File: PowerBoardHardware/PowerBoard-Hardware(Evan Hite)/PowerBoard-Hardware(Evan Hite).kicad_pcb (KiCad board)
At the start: 2 copper layers, 126 parts, among them Q1 IPT020N10N3, Q10 Q_NMOS_DGS, Q11 Q_NMOS_DGS, Q12 Q_NMOS_DGS, Q13 Q_NMOS_DGS, Q2 IPT020N10N3, Q3 IPT020N10N3, Q4 IPT020N10N3, Q5 IPT020N10N3, Q6 Q_NMOS_DGS, Q7 Q_NMOS_DGS, Q8 Q_NMOS_DGS, Q9 Q_NMOS_DGS, U1 TM4C129E_Launchpad, U10 OKI, U11 LT1910, U12 LT1910, U13 LT1910, U14 LT1910, U15 ATC_FUSE_BLOCK, U16 ATC_FUSE_BLOCK, U17 ATC_FUSE_BLOCK, U18 ATC_FUSE_BLOCK, U2 ATC_FUSE_BLOCK, U23 LT1910, U24 LT1910, U25 LT1910, U26 LT1910, U27 ATC_FUSE_BLOCK, U28 ATC_FUSE_BLOCK, U29 ATC_FUSE_BLOCK, U3 ATC_FUSE_BLOCK, U30 ATC_FUSE_BLOCK, U4 ATC_FUSE_BLOCK, U5 LT1910, U6 LT1910

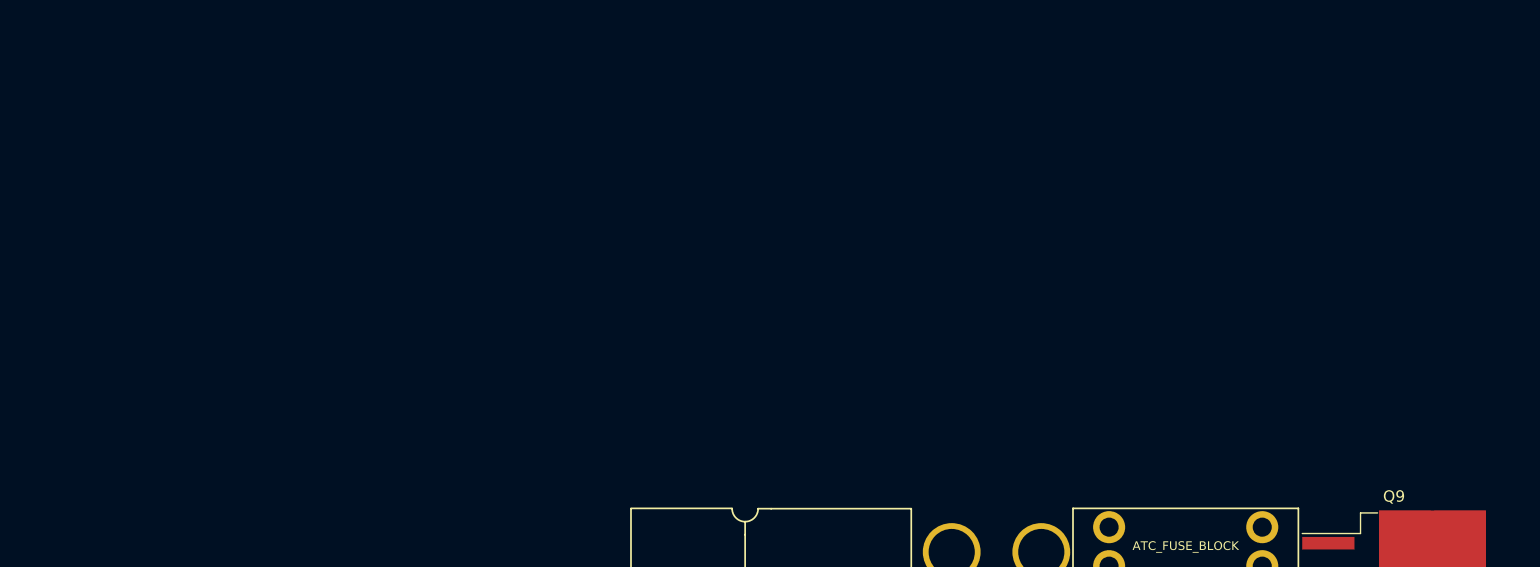
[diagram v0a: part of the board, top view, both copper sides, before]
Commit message: Reassigned Libraries
Reassigned Libraries to make sure everything works after file organization.
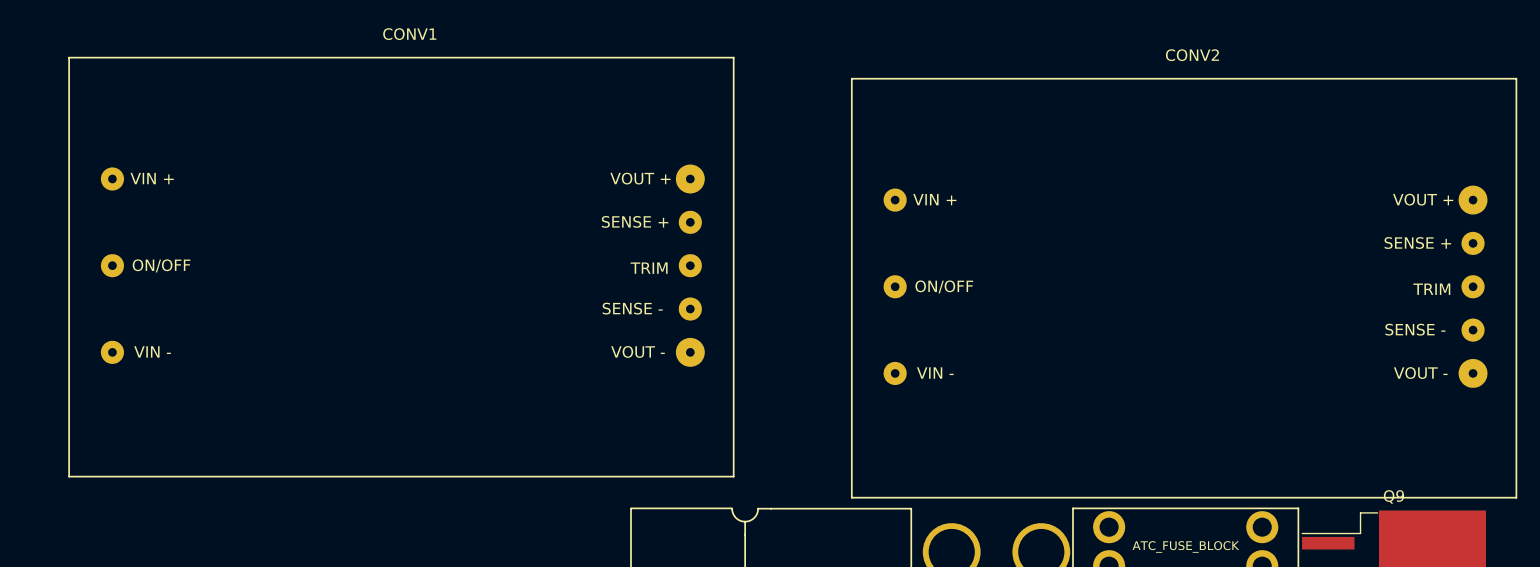
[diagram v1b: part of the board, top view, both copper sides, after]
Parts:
- added CONV1: DC-DC_Converter, DC-DC_Converter_Quarter_Brick:DC-DC_Converter_Quarter_Brick, F.Cu at (177.8, 29.2)
- added CONV2: DC-DC_Converter, DC-DC_Converter_Quarter_Brick:DC-DC_Converter_Quarter_Brick, F.Cu at (246.6, 31.1)
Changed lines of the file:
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@@
     (tracks 0)
     (zones 0)
-    (modules 126)
-    (nets 160)
+    (modules 128)
+    (nets 164)
   )
   (page A4)
@@
     (pad_to_mask_clearance 0.2)
     (aux_axis_origin 0 0)
-    (visible_elements FFFFFF7F)
+    (visible_elements 7FFFFFFF)
     (pcbplotparams
       (layerselection 0x010fc_ffffffff)
@@
   (net 158 "Net-(U26-Pad3)")
   (net 159 "Net-(U26-Pad2)")
+  (net 160 "Net-(CONV1-Pad4)")
+  (net 161 "Net-(CONV1-Pad6)")
+  (net 162 "Net-(CONV2-Pad6)")
+  (net 163 "Net-(CONV2-Pad4)")
   (net_class Default "This is the default net class."
     (clearance 0.2)
@@
     (add_net "Net-(5k8-Pad2)")
     (add_net "Net-(CONV1-Pad2)")
+    (add_net "Net-(CONV1-Pad4)")
+    (add_net "Net-(CONV1-Pad6)")
     (add_net "Net-(CONV2-Pad2)")
+    (add_net "Net-(CONV2-Pad4)")
+    (add_net "Net-(CONV2-Pad6)")
     (add_net "Net-(Q10-Pad2)")
     (add_net "Net-(Q11-Pad2)")
@@
       (net 3 V_BATT))
   )
+  (module DC-DC_Converter_Quarter_Brick:DC-DC_Converter_Quarter_Brick (layer F.Cu)
+    (at 177.8 29.21)
+    (fp_text reference CONV1 (at -24.638 -12.7) (layer F.SilkS)
+      (effects (font (size 1 1) (thickness 0.15)))
+    )
+    (fp_text value DC-DC_Converter (at -24.892 -11.43 180) (layer F.Fab)
+      (effects (font (size 1 1) (thickness 0.15)))
+    )
+    (fp_line (start -54.61 26.162) (end 3.81 26.162) (layer F.SilkS) (width 0.15))
+    (fp_line (start 3.81 -10.668) (end 3.81 26.162) (layer F.SilkS) (width 0.15))
+    (fp_line (start -54.61 -10.668) (end -54.61 26.162) (layer F.SilkS) (width 0.15))
+    (fp_line (start -54.61 -10.668) (end 3.81 -10.668) (layer F.SilkS) (width 0.15))
+    (fp_text user "VIN -" (at -47.244 15.24) (layer F.SilkS)
+      (effects (font (size 1 1) (thickness 0.15)))
+    )
+    (fp_text user ON/OFF (at -46.482 7.62) (layer F.SilkS)
+      (effects (font (size 1 1) (thickness 0.15)))
+    )
+    (fp_text user "VIN +" (at -47.244 0) (layer F.SilkS)
+      (effects (font (size 1 1) (thickness 0.15)))
+    )
+    (fp_text user "VOUT -" (at -4.572 15.24) (layer F.SilkS)
+      (effects (font (size 1 1) (thickness 0.15)))
+    )
+    (fp_text user "VOUT +" (at -4.318 0) (layer F.SilkS)
+      (effects (font (size 1 1) (thickness 0.15)))
+    )
+    (fp_text user "SENSE +" (at -4.826 3.81) (layer F.SilkS)
+      (effects (font (size 1 1) (thickness 0.15)))
+    )
+    (fp_text user TRIM (at -3.556 7.874) (layer F.SilkS)
+      (effects (font (size 1 1) (thickness 0.15)))
+    )
+    (fp_text user "SENSE -" (at -5.08 11.43) (layer F.SilkS)
+      (effects (font (size 1 1) (thickness 0.15)))
+    )
+    (pad 3 thru_hole circle (at -50.8 15.24) (size 2.032 2.032) (drill 0.762) (layers *.Cu *.Mask)
+      (net 1 -BATT))
+    (pad 2 thru_hole circle (at -50.8 7.62) (size 2.032 2.032) (drill 0.762) (layers *.Cu *.Mask)
+      (net 54 "Net-(CONV1-Pad2)"))
+    (pad 1 thru_hole circle (at -50.8 0) (size 2.032 2.032) (drill 0.762) (layers *.Cu *.Mask)
+      (net 3 V_BATT))
+    (pad 4 thru_hole circle (at 0 15.24) (size 2.54 2.54) (drill 0.762) (layers *.Cu *.Mask)
+      (net 160 "Net-(CONV1-Pad4)"))
+    (pad 8 thru_hole circle (at 0 0) (size 2.54 2.54) (drill 0.762) (layers *.Cu *.Mask)
+      (net 34 "Net-(2.2uF1-Pad1)"))
+    (pad 7 thru_hole circle (at 0 3.81) (size 2.032 2.032) (drill 0.762) (layers *.Cu *.Mask)
+      (net 34 "Net-(2.2uF1-Pad1)"))
+    (pad 6 thru_hole circle (at 0 7.62) (size 2.032 2.032) (drill 0.762) (layers *.Cu *.Mask)
+      (net 161 "Net-(CONV1-Pad6)"))
+    (pad 5 thru_hole circle (at 0 11.43) (size 2.032 2.032) (drill 0.762) (layers *.Cu *.Mask)
+      (net 1 -BATT))
+  )
+  (module DC-DC_Converter_Quarter_Brick:DC-DC_Converter_Quarter_Brick (layer F.Cu)
+    (at 246.605001 31.063001)
+    (fp_text reference CONV2 (at -24.638 -12.7) (layer F.SilkS)
+      (effects (font (size 1 1) (thickness 0.15)))
+    )
+    (fp_text value DC-DC_Converter (at -24.892 -11.43 180) (layer F.Fab)
+      (effects (font (size 1 1) (thickness 0.15)))
+    )
+    (fp_text user "SENSE -" (at -5.08 11.43) (layer F.SilkS)
+      (effects (font (size 1 1) (thickness 0.15)))
+    )
+    (fp_text user TRIM (at -3.556 7.874) (layer F.SilkS)
+      (effects (font (size 1 1) (thickness 0.15)))
+    )
+    (fp_text user "SENSE +" (at -4.826 3.81) (layer F.SilkS)
+      (effects (font (size 1 1) (thickness 0.15)))
+    )
+    (fp_text user "VOUT +" (at -4.318 0) (layer F.SilkS)
+      (effects (font (size 1 1) (thickness 0.15)))
+    )
+    (fp_text user "VOUT -" (at -4.572 15.24) (layer F.SilkS)
+      (effects (font (size 1 1) (thickness 0.15)))
+    )
+    (fp_text user "VIN +" (at -47.244 0) (layer F.SilkS)
+      (effects (font (size 1 1) (thickness 0.15)))
+    )
+    (fp_text user ON/OFF (at -46.482 7.62) (layer F.SilkS)
+      (effects (font (size 1 1) (thickness 0.15)))
+    )
+    (fp_text user "VIN -" (at -47.244 15.24) (layer F.SilkS)
+      (effects (font (size 1 1) (thickness 0.15)))
+    )
+    (fp_line (start -54.61 -10.668) (end 3.81 -10.668) (layer F.SilkS) (width 0.15))
+    (fp_line (start -54.61 -10.668) (end -54.61 26.162) (layer F.SilkS) (width 0.15))
+    (fp_line (start 3.81 -10.668) (end 3.81 26.162) (layer F.SilkS) (width 0.15))
+    (fp_line (start -54.61 26.162) (end 3.81 26.162) (layer F.SilkS) (width 0.15))
+    (pad 5 thru_hole circle (at 0 11.43) (size 2.032 2.032) (drill 0.762) (layers *.Cu *.Mask)
+      (net 1 -BATT))
+    (pad 6 thru_hole circle (at 0 7.62) (size 2.032 2.032) (drill 0.762) (layers *.Cu *.Mask)
+      (net 162 "Net-(CONV2-Pad6)"))
+    (pad 7 thru_hole circle (at 0 3.81) (size 2.032 2.032) (drill 0.762) (layers *.Cu *.Mask)
+      (net 36 "Net-(330uF5-Pad1)"))
+    (pad 8 thru_hole circle (at 0 0) (size 2.54 2.54) (drill 0.762) (layers *.Cu *.Mask)
+      (net 36 "Net-(330uF5-Pad1)"))
+    (pad 4 thru_hole circle (at 0 15.24) (size 2.54 2.54) (drill 0.762) (layers *.Cu *.Mask)
+      (net 163 "Net-(CONV2-Pad4)"))
+    (pad 1 thru_hole circle (at -50.8 0) (size 2.032 2.032) (drill 0.762) (layers *.Cu *.Mask)
+      (net 3 V_BATT))
+    (pad 2 thru_hole circle (at -50.8 7.62) (size 2.032 2.032) (drill 0.762) (layers *.Cu *.Mask)
+      (net 55 "Net-(CONV2-Pad2)"))
+    (pad 3 thru_hole circle (at -50.8 15.24) (size 2.032 2.032) (drill 0.762) (layers *.Cu *.Mask)
+      (net 1 -BATT))
+  )
 )

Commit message: Updated Layout
Basic Layout Positioning has begun. DC-DC converters placed. Logic, Actuation, and Communication are placed. One motor has been placed. The rest will be placed at a later time.
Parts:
- added REF**: BATT_PWR_VIA, MRDT-Drill_Holes:BATT_PWR_VIA, F.Cu at (152.9, 128.3)
- added REF**: BATT_PWR_VIA, MRDT-Drill_Holes:BATT_PWR_VIA, F.Cu at (198.6, 128.3)
- added U19: ACS714xLCTR-05B, Housings_SOIC:SOIC-8_3.9x4.9mm_Pitch1.27mm, F.Cu at (255.3, 109.2)
- added U20: ACS714xLCTR-05B, Housings_SOIC:SOIC-8_3.9x4.9mm_Pitch1.27mm, F.Cu at (232.2, 85.2)
- added U21: ACS714xLCTR-05B, Housings_SOIC:SOIC-8_3.9x4.9mm_Pitch1.27mm, F.Cu at (229.9, 194.3)
- added U22: ACS714xLCTR-05B, Housings_SOIC:SOIC-8_3.9x4.9mm_Pitch1.27mm, F.Cu at (229.9, 189.2)
- added U31: ACS714xLCTR-05B, Housings_SOIC:SOIC-8_3.9x4.9mm_Pitch1.27mm, F.Cu at (229.9, 226.1)
- added U32: ACS714xLCTR-05B, Housings_SOIC:SOIC-8_3.9x4.9mm_Pitch1.27mm, F.Cu at (229.9, 221.0)
- added U33: ACS714xLCTR-05B, Housings_SOIC:SOIC-8_3.9x4.9mm_Pitch1.27mm, F.Cu at (229.9, 215.9)
- added U34: ACS714xLCTR-05B, Housings_SOIC:SOIC-8_3.9x4.9mm_Pitch1.27mm, F.Cu at (229.7, 211.2)
- added U7: ACS714xLCTR-05B, Housings_SOIC:SOIC-8_3.9x4.9mm_Pitch1.27mm, F.Cu at (158.8, 20.3)
- added U8: ACS714xLCTR-05B, Housings_SOIC:SOIC-8_3.9x4.9mm_Pitch1.27mm, F.Cu at (224.8, 26.7)
- added U9: ACS714xLCTR-05B, Housings_SOIC:SOIC-8_3.9x4.9mm_Pitch1.27mm, F.Cu at (179.1, 19.1)
- added VCC1: AndersonPP, MRDT-Connectors:Anderson_2_Vertical, F.Cu at (141.7, 24.9)
- added VCC10: AndersonPP, MRDT-Connectors:Anderson_2_Vertical, F.Cu at (27.9, 114.3)
- added VCC11: AndersonPP, MRDT-Connectors:Anderson_2_Vertical, F.Cu at (27.9, 129.5)
- added VCC2: AndersonPP, MRDT-Connectors:Anderson_2_Vertical, F.Cu at (188.2, 24.9)
- added VCC3: AndersonPP, MRDT-Connectors:Anderson_2_Vertical, F.Cu at (236.0, 24.9)
- added VCC4: AndersonPP, MRDT-Connectors:Anderson_2_Vertical, F.Cu at (274.3, 83.8)
- added VCC5: AndersonPP, MRDT-Connectors:Anderson_2_Vertical, F.Cu at (274.3, 102.9)
- added VCC6: AndersonPP, MRDT-Connectors:Anderson_2_Vertical, F.Cu at (274.3, 114.3)
- added VCC7: AndersonPP, MRDT-Connectors:Anderson_2_Vertical, F.Cu at (274.3, 129.5)
- added VCC8: AndersonPP, MRDT-Connectors:Anderson_2_Vertical, F.Cu at (27.9, 83.8)
- added VCC9: AndersonPP, MRDT-Connectors:Anderson_2_Vertical, F.Cu at (27.9, 99.1)
- moved U30 325.1 mm to (372.1, 148.6)
- moved U28 265.4 mm to (351.8, 141.0)
- moved 1.5KE36A2 260.7 mm to (387.4, 121.9)
- moved 1.5KE36A1 239.9 mm to (375.9, 121.9)
- moved U17 206.7 mm to (331.5, 141.0)
- moved Conn5 206.5 mm to (274.3, 102.9), turned to 180 degrees
- moved U27 206.4 mm to (331.5, 148.6)
- moved Conn6 200.7 mm to (274.3, 114.3), turned to 180 degrees
- moved Q12 190.6 mm to (341.9, 184.4)
- moved Conn10 178.4 mm to (27.9, 114.3)
- moved Conn4 177.0 mm to (274.3, 83.8), turned to 180 degrees
- moved 3V3FAN1 165.5 mm to (24.1, 73.7), turned to 90 degrees
- moved 5k1 164.4 mm to (270.5, 73.7)
- moved U2 163.6 mm to (177.8, 49.5), turned to 90 degrees
- moved 1k3 162.2 mm to (227.3, 20.3), turned to 90 degrees
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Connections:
- net -BATT renamed GND
- 0.1uF2 pad 1: V_BATT -> PVDD
- 1.5KE36A1 pad 1: V_BATT -> PVDD
- 1.5KE36A2 pad 1: V_BATT -> PVDD
- 100k3 pad 1: V_BATT -> PVDD
- 10uF2 pad 1: V_BATT -> PVDD
- 1mF1 pad 1: V_BATT -> PVDD
- 1mF2 pad 1: V_BATT -> PVDD
- 1mF3 pad 1: V_BATT -> PVDD
- 1mF4 pad 1: V_BATT -> PVDD
- 1nF2 pad 1: V_BATT -> PVDD
- CONV1 pad 1: V_BATT -> PVDD
- CONV2 pad 1: V_BATT -> PVDD
- U10 pad 1: V_BATT -> PVDD
- U15 pad 1: V_BATT -> PVDD
- U15 pad 2: V_BATT -> Net-(U15-Pad2)
- U16 pad 1: V_BATT -> PVDD
- U16 pad 2: V_BATT -> Net-(U16-Pad2)
- U17 pad 1: V_BATT -> PVDD
- U17 pad 2: V_BATT -> Net-(U17-Pad2)
- U18 pad 1: V_BATT -> PVDD
- U18 pad 2: V_BATT -> Net-(U18-Pad2)
- U2 pad 2: Net-(2.2uF1-Pad1) -> Net-(Q5-Pad3)
- U27 pad 1: V_BATT -> PVDD
- U27 pad 2: V_BATT -> Net-(U27-Pad2)
- U28 pad 1: V_BATT -> PVDD
- U28 pad 2: V_BATT -> Net-(U28-Pad2)
- U29 pad 1: V_BATT -> PVDD
- U29 pad 2: V_BATT -> Net-(U29-Pad2)
- U3 pad 2: Net-(330uF5-Pad1) -> Net-(2.2uF3-Pad1)
- U30 pad 1: V_BATT -> PVDD
- U30 pad 2: V_BATT -> Net-(U30-Pad2)
- U4 pad 2: Net-(2.2uF1-Pad1) -> Net-(Q4-Pad3)
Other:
- copper layers 2 -> 4
- board text added: "<------ Tiva Line Up"

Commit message: 1st Placement is complete
The first placement is now complete, traces still need to be added. The schematic was updated with the placement of Andersons. Certain andersons were in the wrong areas on the schematic. Silkscreen of each motor needs to be added. Outline of board is now in edge cuts.
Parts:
- moved Q12 306.1 mm to (53.7, 81.5)
- moved Q13 297.6 mm to (53.3, 96.5)
- moved Q11 275.5 mm to (53.3, 111.8)
- moved Q10 274.9 mm to (53.7, 127.2)
- moved U30 268.5 mm to (108.0, 100.3), turned to 90 degrees
- moved 1.5KE36A1 259.1 mm to (116.8, 123.2), turned to 270 degrees
- moved 1.5KE36A2 259.1 mm to (128.3, 123.2), turned to 270 degrees
- moved U28 255.4 mm to (99.1, 104.1), turned to 90 degrees
- moved U27 236.6 mm to (99.1, 104.1), turned to 270 degrees
- moved U29 235.0 mm to (82.5, 94.0), turned to 270 degrees
- moved D11 222.4 mm to (15.1, 76.2)
- moved D10 213.3 mm to (15.2, 92.7)
- moved 1mF1 211.0 mm to (119.4, 96.5), turned to 180 degrees
- moved D9 207.9 mm to (15.2, 108.0)
- moved 1mF4 203.4 mm to (128.3, 96.5)
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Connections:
- VCC10 pad 2: Net-(5k8-Pad2) -> Net-(5k6-Pad2)
- VCC11 pad 2: Net-(5k7-Pad2) -> Net-(5k5-Pad2)
- VCC5 pad 2: Net-(5k2-Pad2) -> Net-(5k3-Pad2)
- VCC6 pad 2: Net-(5k3-Pad2) -> Net-(5k4-Pad2)
- VCC7 pad 2: Net-(5k4-Pad2) -> Net-(5k2-Pad2)
- VCC8 pad 2: Net-(5k6-Pad2) -> Net-(5k8-Pad2)
- VCC9 pad 2: Net-(5k5-Pad2) -> Net-(5k7-Pad2)
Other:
- board outline added: 279.4 x 127 mm
- board text removed: "<------ Tiva Line Up"

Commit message: Added Signal Lines
Most of the traces for all signals have been made. Added a pin map file.
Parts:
- moved Conn1 92.9 mm to (234.4, 30.6)
- moved VCC1 92.9 mm to (234.4, 30.6)
- moved Conn2 48.0 mm to (140.6, 30.6)
- moved VCC2 48.0 mm to (140.6, 30.6)
- moved Conn3 47.3 mm to (189.0, 30.6)
- moved VCC3 47.3 mm to (189.0, 30.6)
- moved U13 44.5 mm to (264.8, 77.5)
- moved U4 23.9 mm to (154.3, 52.1), turned to 90 degrees
- moved U3 17.8 mm to (224.8, 48.9)
- moved 0.1uF3 17.3 mm to (165.1, 17.8), turned to 180 degrees
- moved 5k4 8.35 mm to (290.2, 74.9)
- moved Q9 8.28 mm to (278.2, 75.8)
- moved U26 7.62 mm to (68.6, 80.0), turned to 180 degrees
- moved 1k1 6.87 mm to (123.8, 76.2)
- moved 2.2uF2 5.40 mm to (163.5, 40.6)
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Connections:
- U5 pad 4: LOGIC_SIG -> LOGIC-SIG
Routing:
- net IMEAS-M3: track 0.00 -> 308.2 mm, vias 0 -> 7
- net IMEAS-M4: track 0.00 -> 293.1 mm, vias 0 -> 7
- net SIG-M4: track 0.00 -> 268.9 mm, vias 0 -> 4
- net SIG-M2: track 0.00 -> 243.6 mm, vias 0 -> 4
- net SIG-M3: track 0.00 -> 238.1 mm, vias 0 -> 4
- net IMEAS-M2: track 0.00 -> 234.4 mm, vias 0 -> 7
- net SIG-M1: track 0.00 -> 223.1 mm, vias 0 -> 2
- net IMEAS-M1: track 0.00 -> 221.2 mm, vias 0 -> 5
- net IMEAS-ACT: track 0.00 -> 152.2 mm, vias 0 -> 7
- net COM-SIG: track 0.00 -> 114.2 mm, vias 0 -> 4
- net SIG-AUX: track 0.00 -> 102.6 mm, vias 0 -> 3
- net Net-(CONV2-Pad2): track 0.00 -> 102.1 mm, vias 0 -> 1
- net IMEAS-M5: track 0.00 -> 88.1 mm, vias 0 -> 3
- net IMEAS-M6: track 0.00 -> 86.8 mm, vias 0 -> 3
- net SIG-M7: track 0.00 -> 83.6 mm, vias 0 -> 3
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- added copper zone on BM.Cu, net GND
- added copper zone on F.Cu, net Net-(2.2uF1-Pad1)
- added copper zone on F.Cu, net Net-(330uF5-Pad1)
- added copper zone on F.Cu, net PVDD
- added copper zone on UM.Cu, net PVDD

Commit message: Updated Pin Map and Added New Vertical Anderson Package
Updated pin map to have accurate information. Updated outgoing pins to be more precise. Added the vertical anderson for a more accurate layout. Split ground plane to prevent Ground looping.
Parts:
- removed VCC1, VCC10, VCC11, VCC2, VCC3, VCC4, VCC5, VCC6, VCC7, VCC8, VCC9: AndersonPP, MRDT-Connectors:Anderson_2_Vertical
- Conn1, Conn2, Conn3: footprint MRDT-Connectors:Anderson_2_Vertical -> Vertical Anderson Double:Vertical Anderson Double
- moved Q6 25.5 mm to (278.4, 75.7), turned to 0 degrees
- moved 5k3 25.2 mm to (288.0, 76.2)
- moved Q9 24.0 mm to (270.3, 53.1), turned to 0 degrees
- moved D7 23.4 mm to (288.9, 57.9)
- moved D6 21.4 mm to (290.1, 79.8), turned to 90 degrees
- moved 5k4 20.9 mm to (286.5, 54.4), turned to 180 degrees
- moved 2.2uF1 14.7 mm to (186.1, 53.3)
- moved 1k4 14.6 mm to (161.9, 14.8)
- moved 5k1 9.61 mm to (281.9, 34.9)
- moved 2.2uF3 8.64 mm to (214.6, 32.4)
- moved 1nF5 5.71 mm to (212.1, 24.8)
- moved 0.1uF6 5.12 mm to (242.6, 57.8), turned to 90 degrees
- moved 5k2 5.00 mm to (284.0, 103.6), turned to 180 degrees
- moved Q8 4.62 mm to (270.5, 29.8), turned to 0 degrees
- moved 0.1uF7 4.49 mm to (252.1, 57.8), turned to 90 degrees
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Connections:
- net SER_RX renamed Net-(U1-PadPC4)
- net SER_TX renamed Net-(U1-PadPC5)
- CONV1 pad 4: Net-(CONV1-Pad4) -> GND
- Conn1 pad 2: (no net) -> Net-(1k3-Pad2)
- Conn10 pad 2: (no net) -> Net-(5k6-Pad2)
- Conn11 pad 2: (no net) -> Net-(5k5-Pad2)
- Conn2 pad 2: (no net) -> Net-(1k4-Pad2)
- Conn3 pad 2: (no net) -> Net-(1k5-Pad2)
- Conn4 pad 2: (no net) -> Net-(5k1-Pad2)
- Conn5 pad 2: (no net) -> Net-(5k3-Pad2)
- Conn6 pad 2: (no net) -> Net-(5k4-Pad2)
- Conn7 pad 2: (no net) -> Net-(5k2-Pad2)
- Conn8 pad 2: (no net) -> Net-(5k8-Pad2)
- Conn9 pad 2: (no net) -> Net-(5k7-Pad2)
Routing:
- net Net-(0.1uF8-Pad1): track 0.00 -> 69.0 mm, vias 0 -> 2
- net IMEAS-COM: track 60.7 -> 26.5 mm
- net Net-(Q5-Pad2): track 0.00 -> 24.1 mm, vias 0 -> 2
- net 3.3V: track 6.93 -> 27.2 mm
- net IMEAS-ACT: track 152.2 -> 140.0 mm, vias 7 -> 9
- net Net-(Q4-Pad2): track 0.00 -> 10.0 mm, vias 0 -> 2
- net Net-(0.1uF7-Pad1): track 0.00 -> 9.58 mm
- net Net-(1k5-Pad2): track 0.00 -> 8.50 mm
- net Net-(1k4-Pad1): track 0.00 -> 8.50 mm
- net Net-(Q5-Pad1): track 0.00 -> 7.20 mm
- net Net-(1k3-Pad2): track 0.00 -> 5.91 mm
- net Net-(5k3-Pad1): track 0.00 -> 5.24 mm
- net Net-(0.1uF9-Pad1): track 0.00 -> 5.17 mm
- net Net-(0.1uF6-Pad1): track 0.00 -> 5.14 mm
- net Net-(5k1-Pad1): track 0.00 -> 4.69 mm
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- added copper zone on F.Cu, net Net-(1k3-Pad2)
- added copper zone on F.Cu, net Net-(1k4-Pad2)
- added copper zone on F.Cu, net Net-(1k5-Pad2)
- added copper zone on F.Cu, net Net-(2.2uF3-Pad1)
- added copper zone on F.Cu, net Net-(5k1-Pad2)
- added copper zone on F.Cu, net Net-(5k2-Pad2)
- added copper zone on F.Cu, net Net-(5k3-Pad2)
- added copper zone on F.Cu, net Net-(5k4-Pad2)
- added copper zone on F.Cu, net Net-(5k5-Pad2)
- added copper zone on F.Cu, net Net-(5k6-Pad2)
- added copper zone on F.Cu, net Net-(5k7-Pad2)
- added copper zone on F.Cu, net Net-(5k8-Pad2)
- added copper zone on F.Cu, net Net-(Q4-Pad3)
- added copper zone on F.Cu, net Net-(Q5-Pad3)
- added copper zone on F.Cu, net Net-(U15-Pad2)
- added copper zone on F.Cu, net Net-(U16-Pad2)
- added copper zone on F.Cu, net Net-(U17-Pad2)
- added copper zone on F.Cu, net Net-(U18-Pad2)
- added copper zone on F.Cu, net Net-(U27-Pad2)
- added copper zone on F.Cu, net Net-(U28-Pad2)
- added copper zone on F.Cu, net Net-(U29-Pad2)
- added copper zone on F.Cu, net Net-(U30-Pad2)
